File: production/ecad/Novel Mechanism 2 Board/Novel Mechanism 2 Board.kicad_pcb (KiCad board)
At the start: 2 copper layers, 14 parts, among them J1 1755736, J2 1755736, U1 L9958SBTR

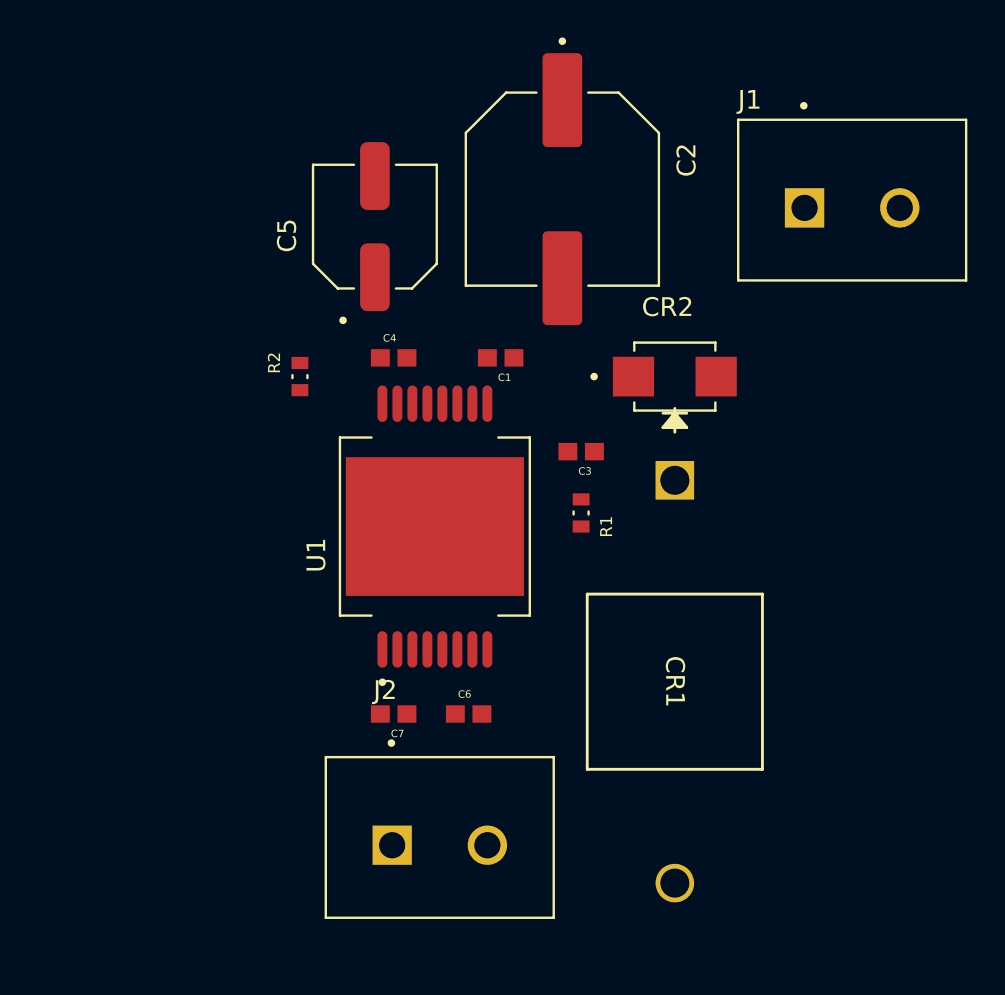
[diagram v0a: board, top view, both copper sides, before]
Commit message: added component to layout
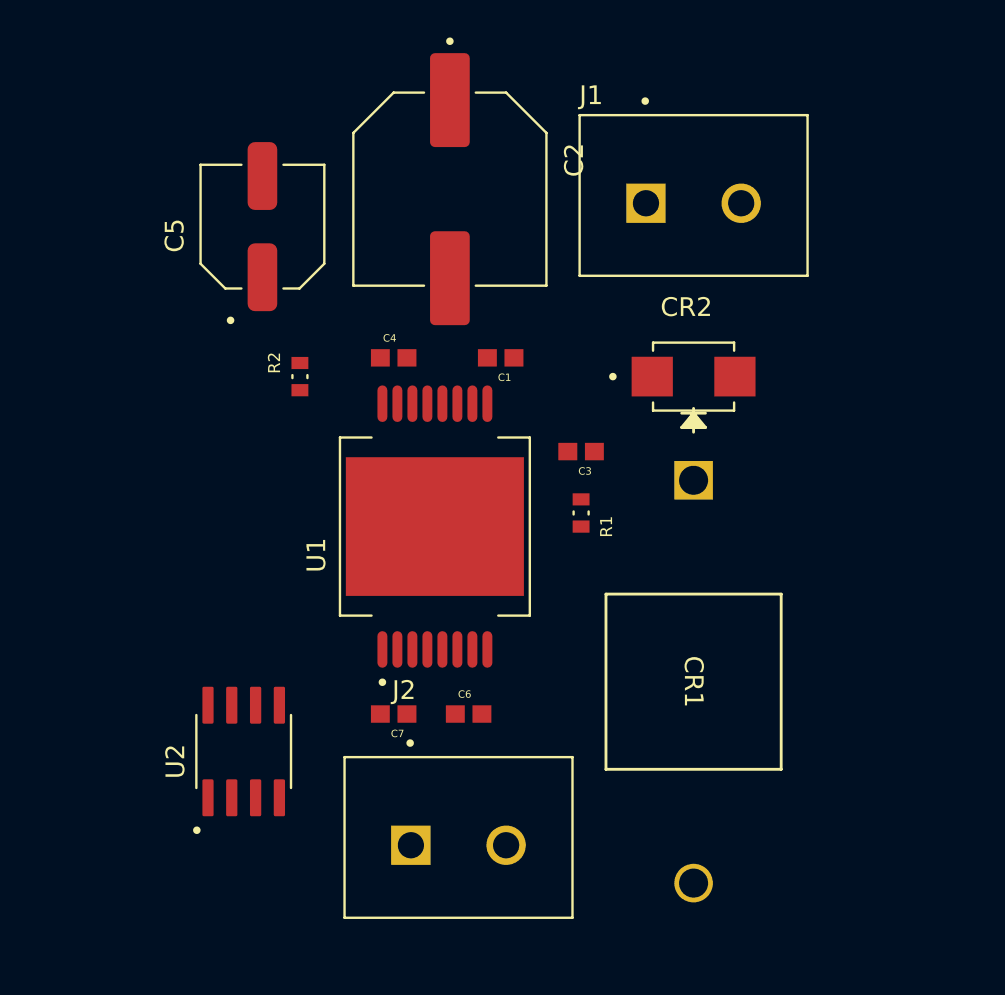
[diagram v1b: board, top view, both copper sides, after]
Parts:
- added U2: TMCS1108A4BQDRQ1, Package_SO:TMCS1108A4BQDRQ1, F.Cu at (127.0, 82.0)
- moved J1 8.46 mm to (144.9, 56.6)
- moved C2 6.00 mm to (138.0, 52.0)
- moved C5 6.00 mm to (128.0, 54.0)
- moved CR1 1.00 mm to (151.0, 67.5)
- moved CR2 1.00 mm to (151.0, 62.0)
- moved J2 1.00 mm to (132.4, 90.9)
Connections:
- J2 pad 2: Net-(U1-OUT1) -> Net-(U2-IN-)
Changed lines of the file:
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@@
   (net 16 "/SI")
   (net 17 "/SCK")
+  (net 18 "Net-(U2-IN-)")
+  (net 19 "unconnected-(U2-NC-Pad6)")
+  (net 20 "/AOUT")
   (footprint "Diode_SMD:STTH4R02U" (layer "F.Cu")
-    (at 150 62)
+    (at 151 62)
     (property "Sheetfile" "Novel Mechanism 2 Board.kicad_sch")
     (property "Sheetname" "")
@@
   )
   (footprint "Connector:PHOENIX_1755736" (layer "F.Cu")
-    (at 153.38 56.87)
+    (at 144.92 56.6225)
     (property "MANUFACTURER" "Phoenix Contact")
     (property "MAXIMUM_PACKAGE_HEIGHT" "12.15mm")
@@
       (net 5 "GND") (pintype "passive") (solder_mask_margin 0.102))
   )
+  (footprint "Package_SO:TMCS1108A4BQDRQ1" (layer "F.Cu")
+    (at 127 82 90)
+    (property "A1_MIN" "0.11")
+    (property "A_MAX" "1.75")
+    (property "A_MIN" "1.75")
+    (property "A_NOM" "1.75")
+    (property "B_MAX" "0.51")
+    (property "B_MIN" "0.31")
+    (property "B_NOM" "0.41")
+    (property "D1_MAX" "")
+    (property "D1_MIN" "")
+    (property "D1_NOM" "")
+    (property "D2_MAX" "0.0")
+    (property "DMAX" "")
+    (property "DMIN" "")
+    (property "DNOM" "")
+    (property "D_MAX" "5.0")
+    (property "D_MIN" "4.81")
+    (property "D_NOM" "4.905")
+    (property "E1_MAX" "3.98")
+    (property "E1_MIN" "3.81")
+    (property "E1_NOM" "3.895")
+    (property "E2_MAX" "0.0")
+    (property "EMAX" "")
+    (property "EMIN" "")
+    (property "ENOM" "1.27")
+    (property "E_MAX" "6.19")
+    (property "E_MIN" "5.8")
+    (property "E_NOM" "5.995")
+    (property "L1_MAX" "")
+    (property "L1_MIN" "")
+    (property "L1_NOM" "")
+    (property "L_MAX" "1.27")
+    (property "L_MIN" "0.41")
+    (property "L_NOM" "0.84")
+    (property "MANUFACTURER" "Texas Instruments")
+    (property "PACKAGE_TYPE" "")
+    (property "PARTREV" "July 2021")
+    (property "PINS" "")
+    (property "PIN_COUNT" "8.0")
+    (property "SNAPEDA_PACKAGE_ID" "")
+    (property "STANDARD" "IPC 7351B")
+    (property "Sheetfile" "Novel Mechanism 2 Board.kicad_sch")
+    (property "Sheetname" "")
+    (property "VACANCIES" "")
+    (attr smd)
+    (fp_text reference "U2" (at -0.53 -3.635 90) (layer "F.SilkS")
+        (effects (font (size 1 1) (thickness 0.15)))
+    )
+    (fp_text value "TMCS1108A4BQDRQ1" (at 7.725 3.635 90) (layer "F.Fab")
+        (effects (font (size 1 1) (thickness 0.15)))
+    )
+    (fp_line (start -1.9475 -2.525) (end 1.9475 -2.525)
+      (stroke (width 0.127) (type solid)) (layer "F.SilkS"))
+    (fp_line (start -1.9475 2.525) (end 1.9475 2.525)
+      (stroke (width 0.127) (type solid)) (layer "F.SilkS"))
+    (fp_circle (center -4.2 -2.5) (end -4.1 -2.5)
+      (stroke (width 0.2) (type solid)) (fill none) (layer "F.SilkS"))
+    (fp_line (start -3.705 -2.7025) (end -3.705 2.7025)
+      (stroke (width 0.05) (type solid)) (layer "F.CrtYd"))
+    (fp_line (start -3.705 -2.7025) (end 3.705 -2.7025)
+      (stroke (width 0.05) (type solid)) (layer "F.CrtYd"))
+    (fp_line (start -3.705 2.7025) (end 3.705 2.7025)
+      (stroke (width 0.05) (type solid)) (layer "F.CrtYd"))
+    (fp_line (start 3.705 -2.7025) (end 3.705 2.7025)
+      (stroke (width 0.05) (type solid)) (layer "F.CrtYd"))
+    (fp_line (start -1.9475 -2.4525) (end -1.9475 2.4525)
+      (stroke (width 0.127) (type solid)) (layer "F.Fab"))
+    (fp_line (start -1.9475 -2.4525) (end 1.9475 -2.4525)
+      (stroke (width 0.127) (type solid)) (layer "F.Fab"))
+    (fp_line (start -1.9475 2.4525) (end 1.9475 2.4525)
+      (stroke (width 0.127) (type solid)) (layer "F.Fab"))
+    (fp_line (start 1.9475 -2.4525) (end 1.9475 2.4525)
+      (stroke (width 0.127) (type solid)) (layer "F.Fab"))
+    (fp_circle (center -4.2 -2.5) (end -4.1 -2.5)
+      (stroke (width 0.2) (type solid)) (fill none) (layer "F.Fab"))
+    (pad "1" smd roundrect (at -2.47 -1.905 90) (size 1.97 0.6) (layers "F.Cu" "F.Paste" "F.Mask") (roundrect_rratio 0.125)
+      (net 6 "Net-(U1-OUT1)") (pinfunction "IN+") (pintype "input") (solder_mask_margin 0.102))
+    (pad "2" smd roundrect (at -2.47 -0.635 90) (size 1.97 0.6) (layers "F.Cu" "F.Paste" "F.Mask") (roundrect_rratio 0.125)
+      (net 6 "Net-(U1-OUT1)") (pinfunction "IN+__1") (pintype "input") (solder_mask_margin 0.102))
+    (pad "3" smd roundrect (at -2.47 0.635 90) (size 1.97 0.6) (layers "F.Cu" "F.Paste" "F.Mask") (roundrect_rratio 0.125)
+      (net 18 "Net-(U2-IN-)") (pinfunction "IN-") (pintype "input") (solder_mask_margin 0.102))
+    (pad "4" smd roundrect (at -2.47 1.905 90) (size 1.97 0.6) (layers "F.Cu" "F.Paste" "F.Mask") (roundrect_rratio 0.125)
+      (net 18 "Net-(U2-IN-)") (pinfunction "IN-__1") (pintype "input") (solder_mask_margin 0.102))
+    (pad "5" smd roundrect (at 2.47 1.905 90) (size 1.97 0.6) (layers "F.Cu" "F.Paste" "F.Mask") (roundrect_rratio 0.125)
+      (net 5 "GND") (pinfunction "GND") (pintype "power_in") (solder_mask_margin 0.102))
+    (pad "6" smd roundrect (at 2.47 0.635 90) (size 1.97 0.6) (layers "F.Cu" "F.Paste" "F.Mask") (roundrect_rratio 0.125)
+      (net 19 "unconnected-(U2-NC-Pad6)") (pinfunction "NC") (pintype "no_connect") (solder_mask_margin 0.102))
+    (pad "7" smd roundrect (at 2.47 -0.635 90) (size 1.97 0.6) (layers "F.Cu" "F.Paste" "F.Mask") (roundrect_rratio 0.125)
+      (net 20 "/AOUT") (pinfunction "VOUT") (pintype "output") (solder_mask_margin 0.102))
+    (pad "8" smd roundrect (at 2.47 -1.905 90) (size 1.97 0.6) (layers "F.Cu" "F.Paste" "F.Mask") (roundrect_rratio 0.125)
+      (net 4 "+5V") (pinfunction "VS") (pintype "power_in") (solder_mask_margin 0.102))
+  )
   (footprint "Capacitor_SMD:EDK106M050A9GAA" (layer "F.Cu")
-    (at 134 54 90)
+    (at 128 54 90)
     (property "Sheetfile" "Novel Mechanism 2 Board.kicad_sch")
     (property "Sheetname" "")
@@
         (effects (font (size 0.64 0.64) (thickness 0.15)))
     )
-    (fp_text value "10k" (at 5.2024 1.3564 90) (layer "F.Fab")
+    (fp_text value "10k" (at 5.2024 -4.6436 90) (layer "F.Fab")
         (effects (font (size 0.64 0.64) (thickness 0.15)))
     )
@@
   )
   (footprint "Diode_THT:BZW50-27B" (layer "F.Cu")
-    (at 150 67.53215 -90)
+    (at 151 67.53215 -90)
     (tags "BZW50-27B ")
     (property "Sheetfile" "Novel Mechanism 2 Board.kicad_sch")
@@
   )
   (footprint "Connector:PHOENIX_1755736" (layer "F.Cu")
-    (at 131.38 90.87)
+    (at 132.38 90.87)
     (property "MANUFACTURER" "Phoenix Contact")
     (property "MAXIMUM_PACKAGE_HEIGHT" "12.15mm")
@@
       (net 7 "Net-(U1-OUT2)") (pinfunction "1") (pintype "passive") (solder_mask_margin 0.102))
     (pad "2" thru_hole circle (at 8.62 -3.87) (size 2.1 2.1) (drill 1.4) (layers "*.Cu" "*.Mask")
-      (net 6 "Net-(U1-OUT1)") (pinfunction "2") (pintype "passive") (solder_mask_margin 0.102))
+      (net 18 "Net-(U2-IN-)") (pinfunction "2") (pintype "passive") (solder_mask_margin 0.102))
   )
   (footprint "Capacitor_SMD:CAP_0603" (layer "F.Cu")
@@
   )
   (footprint "Capacitor_SMD:EDK107M063A9PAA" (layer "F.Cu")
-    (at 144 52 -90)
-    (property "Sheetfile" "Novel Mechanism 2 Board.kicad_sch")
-    (property "Sheetname" "")
+    (at 138 52 -90)
+    (property "Sheetfile" "Novel Mechanism 2 Board.kicad_sch")
+    (property "Sheetname" "")

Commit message: basically final component placement
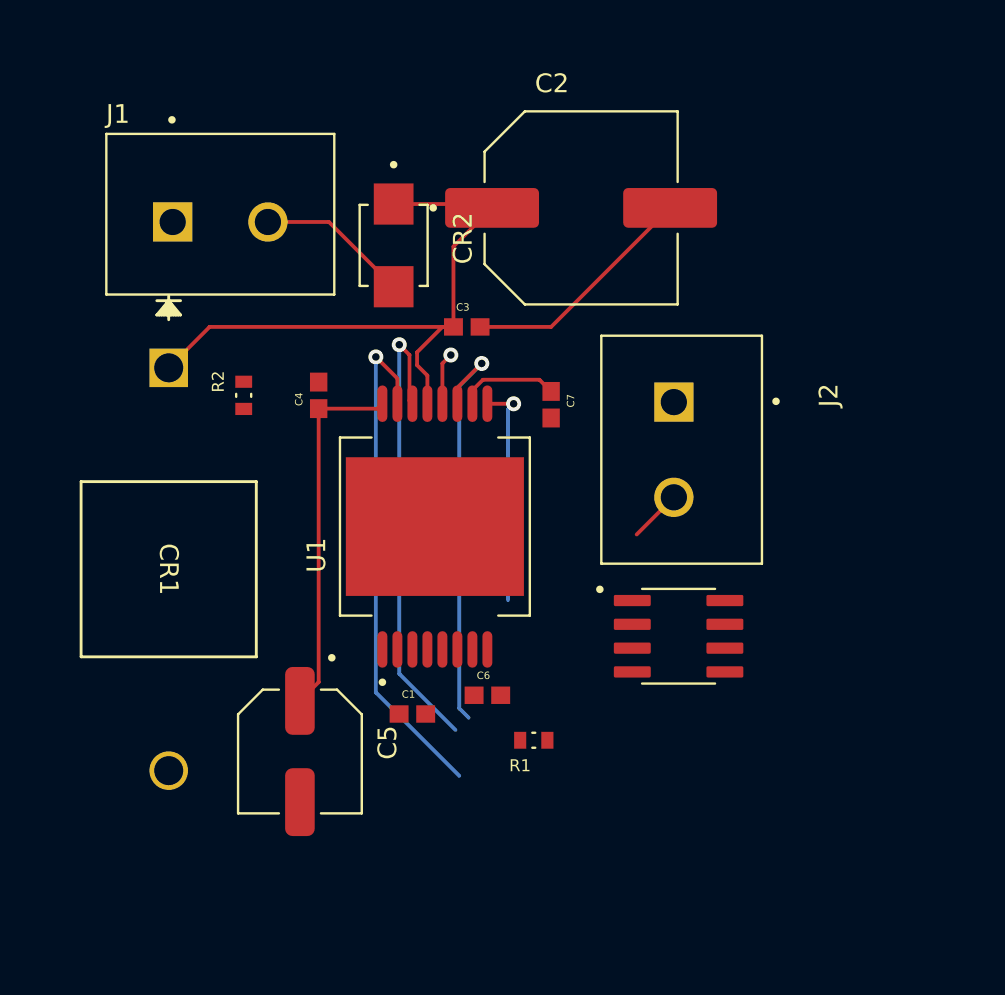
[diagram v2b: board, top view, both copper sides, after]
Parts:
- moved J2 33.9 mm to (146.1, 59.8), turned to -90 degrees
- moved CR1 28.6 mm to (123.0, 61.5)
- moved C5 28.1 mm to (130.0, 82.0), turned to -90 degrees
- moved J1 25.3 mm to (119.7, 57.6)
- moved U2 24.0 mm to (150.2, 75.8), turned to 0 degrees
- moved C1 19.6 mm to (136.0, 80.0), turned to 0 degrees
- moved C7 18.5 mm to (143.4, 63.5), turned to -90 degrees
- moved CR2 17.5 mm to (135.0, 55.0), turned to -90 degrees
- moved R1 12.4 mm to (142.5, 81.4), turned to 180 degrees
- moved C3 9.02 mm to (138.9, 59.4), turned to 0 degrees
- moved C2 7.07 mm to (145.0, 53.0), turned to 0 degrees
- moved C4 4.47 mm to (131.0, 63.0), turned to 90 degrees
- moved R2 3.16 mm to (127.0, 63.0)
- moved C6 1.41 mm to (140.0, 79.0)
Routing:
- net +15V: track 0.00 -> 34.1 mm
- net /SCK: track 0.00 -> 27.2 mm, vias 0 -> 1
- net /SI: track 0.00 -> 25.2 mm, vias 0 -> 1
- net /PWM: track 0.00 -> 22.3 mm, vias 0 -> 1
- net +5V: track 0.00 -> 19.7 mm
- net Net-(C2-Pad2): track 0.00 -> 12.8 mm
- net /Enable: track 0.00 -> 12.7 mm, vias 0 -> 1
- net Net-(CR2-Pad2): track 0.00 -> 8.14 mm
- net Net-(U1-OUT2): track 0.00 -> 5.40 mm
- net Net-(U2-IN-): track 0.00 -> 2.80 mm
- net Net-(U1-REXT): track 0.00 -> 2.78 mm, vias 0 -> 1
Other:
- rule pad_to_mask_clearance: 0 -> 0.05

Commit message: imported updated schematic
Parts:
- added J3: 0532611271, Connector:MOLEX_0532611271, F.Cu at (145.2, 87.4)
- added R3: 10k, Resistor_SMD:RES_0603, F.Cu at (151.0, 80.8)
- added R4: 10k, Resistor_SMD:RES_0603, F.Cu at (147.8, 80.8)
- added R5: 50k, Resistor_SMD:RES_0603, F.Cu at (145.8, 80.8)
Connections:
- C2 pad 2: Net-(C2-Pad2) -> GND
- C3 pad 2: Net-(C2-Pad2) -> GND
- U2 pad 7: /AOUT -> Net-(U2-VOUT)
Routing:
- net Net-(C2-Pad2): track 12.8 -> 0.00 mm
- net GND: track 0.00 -> 12.8 mm

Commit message: edge cuts
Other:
- board outline added: 41.7 x 46.1 mm
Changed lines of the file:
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@@
     (property "Sheetname" "")
     (attr through_hole)
-    (fp_text reference "J2" (at 3.175 -12.135 90) (layer "F.SilkS")
+    (fp_text reference "J2" (at -1.77 -6.4725 90) (layer "F.SilkS")
         (effects (font (size 1 1) (thickness 0.15)))
     )
@@
       (net 24 "unconnected-(J3-SHIELD__1-PadS2)") (pinfunction "SHIELD__1") (pintype "passive") (solder_mask_margin 0.0762))
   )
+  (gr_rect (start 116.95 46) (end 158.7 92.1)
+    (stroke (width 0.2) (type default)) (fill none) (layer "Edge.Cuts"))
   (segment (start 136.8 63.445) (end 136.8 61.942213) (width 0.2032) (layer "F.Cu") (net 1))
   (segment (start 138.191 59.35) (end 138.191 55.059) (width 0.2032) (layer "F.Cu") (net 1))
